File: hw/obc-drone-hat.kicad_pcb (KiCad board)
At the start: 2 copper layers, 65 x 56.5 mm, 0 parts

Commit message: hw: wonring on NET
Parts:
- added C1: 0.1, Capacitor_SMD:C_0603_1608Metric, F.Cu at (270.9, 119.1)
- added C10: 0.1, Capacitor_SMD:C_0603_1608Metric, F.Cu at (284.8, 105.7)
- added C11: 0.1, Capacitor_SMD:C_0603_1608Metric, F.Cu at (339.0, 99.8)
- added C12: 0.1, Capacitor_SMD:C_0603_1608Metric, F.Cu at (347.7, 94.1)
- added C13: 0.1, Capacitor_SMD:C_0603_1608Metric, F.Cu at (335.6, 99.8)
- added C14: 0.1, Capacitor_SMD:C_0603_1608Metric, F.Cu at (303.1, 117.5)
- added C15: 0.01, Capacitor_SMD:C_0603_1608Metric, F.Cu at (286.8, 81.6)
- added C16: 10.0 50V, Capacitor_SMD:C_1206_3216Metric_Pad1.24x1.80mm_HandSolder, F.Cu at (252.7, 84.1)
- added C17: 10.0 50V, Capacitor_SMD:C_1206_3216Metric_Pad1.24x1.80mm_HandSolder, F.Cu at (271.4, 82.4)
- added C18: 0.47, Capacitor_SMD:C_1206_3216Metric_Pad1.24x1.80mm_HandSolder, F.Cu at (259.1, 84.1)
- added C19: 1000.0 uF 10 V, Capacitor_SMD:CP_Elec_10x10.5, F.Cu at (188.0, 99.0)
- added C2: 0.1, Capacitor_SMD:C_0603_1608Metric, F.Cu at (291.6, 108.5)
- added C3: 0.1, Capacitor_SMD:C_0603_1608Metric, F.Cu at (293.2, 97.8)
- added C4: 0.1, Capacitor_SMD:C_0603_1608Metric, F.Cu at (277.7, 116.7)
- added C5: 0.1, Capacitor_SMD:C_0603_1608Metric, F.Cu at (270.9, 113.7)
- added C6: 0.1, Capacitor_SMD:C_0603_1608Metric, F.Cu at (293.2, 103.2)
- added C7: 0.1, Capacitor_SMD:C_0603_1608Metric, F.Cu at (296.6, 97.8)
- added C8: 0.1, Capacitor_SMD:C_0603_1608Metric, F.Cu at (282.8, 111.0)
- added C9: 0.1, Capacitor_SMD:C_0603_1608Metric, F.Cu at (288.2, 105.7)
- added DA1: NCP361SN, Package_TO_SOT_SMD:SOT-23-5_HandSoldering, F.Cu at (287.3, 99.1)
- added DA2: LM2678SX-5.0/NOPB, Package_TO_SOT_SMD:TO-263-7_TabPin4, F.Cu at (185.0, 125.0)
- added DD1: CAT24C256WI-GT3, Package_SO:SO-8_5.3x6.2mm_P1.27mm, F.Cu at (308.6, 100.3)
- added DD2: STM32F030CCTx, Package_QFP:LQFP-48_7x7mm_P0.5mm, F.Cu at (281.0, 138.0)
- added DD3: NC7SZ157P6X, Package_TO_SOT_SMD:SOT-363_SC-70-6_Handsoldering, F.Cu at (267.2, 108.0)
- added DD4: MAX3109, Package_DFN_QFN:QFN-32-1EP_5x5mm_P0.5mm_EP3.45x3.45mm, F.Cu at (337.4, 153.7)
- added DD5: DS3231, Package_SO:SOIC-16W_7.5x10.3mm_P1.27mm, F.Cu at (350.6, 156.2)
- added HL1: WS2812B, LED_SMD:LED_WS2812B_PLCC4_5.0x5.0mm_P3.2mm, F.Cu at (265.3, 115.6)
- added JP1: Jumper_3_Open, Jumper:SolderJumper-3_P1.3mm_Open_RoundedPad1.0x1.5mm, F.Cu at (339.9, 94.2)
- added L1: 12 uH SRR1208-120ML, Inductor_SMD:L_12x12mm_H8mm, F.Cu at (187.0, 111.0)
- added R1: 1k, Resistor_SMD:R_0603_1608Metric, F.Cu at (303.0, 108.1)
- added R10: 10k, Resistor_SMD:R_0603_1608Metric, F.Cu at (284.4, 116.4)
- added R11: 10k, Resistor_SMD:R_0603_1608Metric, F.Cu at (286.2, 111.0)
- added R12: 10k, Resistor_SMD:R_0603_1608Metric, F.Cu at (295.1, 113.9)
- added R13: 4.7k, Resistor_SMD:R_0603_1608Metric, F.Cu at (291.5, 113.9)
- added R14: 10k, Resistor_SMD:R_0603_1608Metric, F.Cu at (287.9, 116.4)
- added R15: nc, Resistor_SMD:R_0603_1608Metric, F.Cu at (347.7, 99.4)
- added R16: 10k, Resistor_SMD:R_0603_1608Metric, F.Cu at (342.5, 99.8)
- added R2: 3.9k, Resistor_SMD:R_0603_1608Metric, F.Cu at (317.7, 105.7)
- added R3: 3.9k, Resistor_SMD:R_0603_1608Metric, F.Cu at (306.6, 108.1)
- added R4: 10k, Resistor_SMD:R_0603_1608Metric, F.Cu at (325.9, 97.8)
- added R5: 47k, Resistor_SMD:R_0603_1608Metric, F.Cu at (310.1, 108.1)
- added R6: 47k, Resistor_SMD:R_0603_1608Metric, F.Cu at (294.9, 108.5)
- added R7: 10k, Resistor_SMD:R_0603_1608Metric, F.Cu at (274.3, 116.7)
- added R8: 47k, Resistor_SMD:R_0603_1608Metric, F.Cu at (296.6, 103.2)
- added R9: 10k, Resistor_SMD:R_0603_1608Metric, F.Cu at (281.0, 116.7)
- added SW1: SW_DIP_x04, Button_Switch_THT:SW_DIP_SPSTx04_Slide_9.78x12.34mm_W7.62mm_P2.54mm, F.Cu at (154.0, 93.0)
- added VT1: DMG2305UX, Package_TO_SOT_SMD:SOT-23_Handsoldering, F.Cu at (368.5, 116.5)
- added VT2: DMMT5401, Package_TO_SOT_SMD:SOT-23-6_Handsoldering, F.Cu at (320.0, 99.1)
- added VT3: DMG2305UX, Package_TO_SOT_SMD:SOT-23_Handsoldering, F.Cu at (368.5, 126.6)
- added XP11: UNUSED PINS, Connector_PinSocket_2.00mm:PinSocket_2x05_P2.00mm_Vertical, F.Cu at (327.0, 59.0)
- added XP12: PWR-5V, Connector_JST:JST_PH_B2B-PH-K_1x02_P2.00mm_Vertical, F.Cu at (338.8, 67.9)
- added XP13: PWR-5V, Connector_JST:JST_PH_B2B-PH-K_1x02_P2.00mm_Vertical, F.Cu at (339.0, 76.0)
- added XP2: FrSky-XSR, Connector_JST:JST_GH_SM06B-GHS-TB_1x06-1MP_P1.25mm_Horizontal, F.Cu at (150.0, 137.0)
- added XP3: DC-Debug, Connector_JST:JST_GH_BM06B-GHS-TBT_1x06-1MP_P1.25mm_Vertical, F.Cu at (225.0, 89.0)
- added XP4: FAN, Connector:FanPinHeader_1x03_P2.54mm_Vertical, F.Cu at (276.0, 99.6)
- added XP5: CPPM OUT, Connector_JST:JST_PH_B2B-PH-K_1x02_P2.00mm_Vertical, F.Cu at (159.0, 136.0)
- added XP6: TELEM1, Connector_JST:JST_GH_SM06B-GHS-TB_1x06-1MP_P1.25mm_Horizontal, F.Cu at (134.0, 97.0)
- added XP7: TELEM2, Connector_JST:JST_GH_SM06B-GHS-TB_1x06-1MP_P1.25mm_Horizontal, F.Cu at (134.0, 109.0)
- added XP8: CFG ID, Connector_JST:JST_PH_B4B-PH-K_1x04_P2.00mm_Vertical, F.Cu at (160.0, 94.0)
- added XP9: RPI-CON, Connector_JST:JST_GH_BM06B-GHS-TBT_1x06-1MP_P1.25mm_Vertical, F.Cu at (213.0, 89.0)
- added ZQ1: ASFL1-24.000MHZ-EC-T, Crystal:Crystal_SMD_Abracon_ABM3B-4Pin_5.0x3.2mm, F.Cu at (323.9, 152.8)

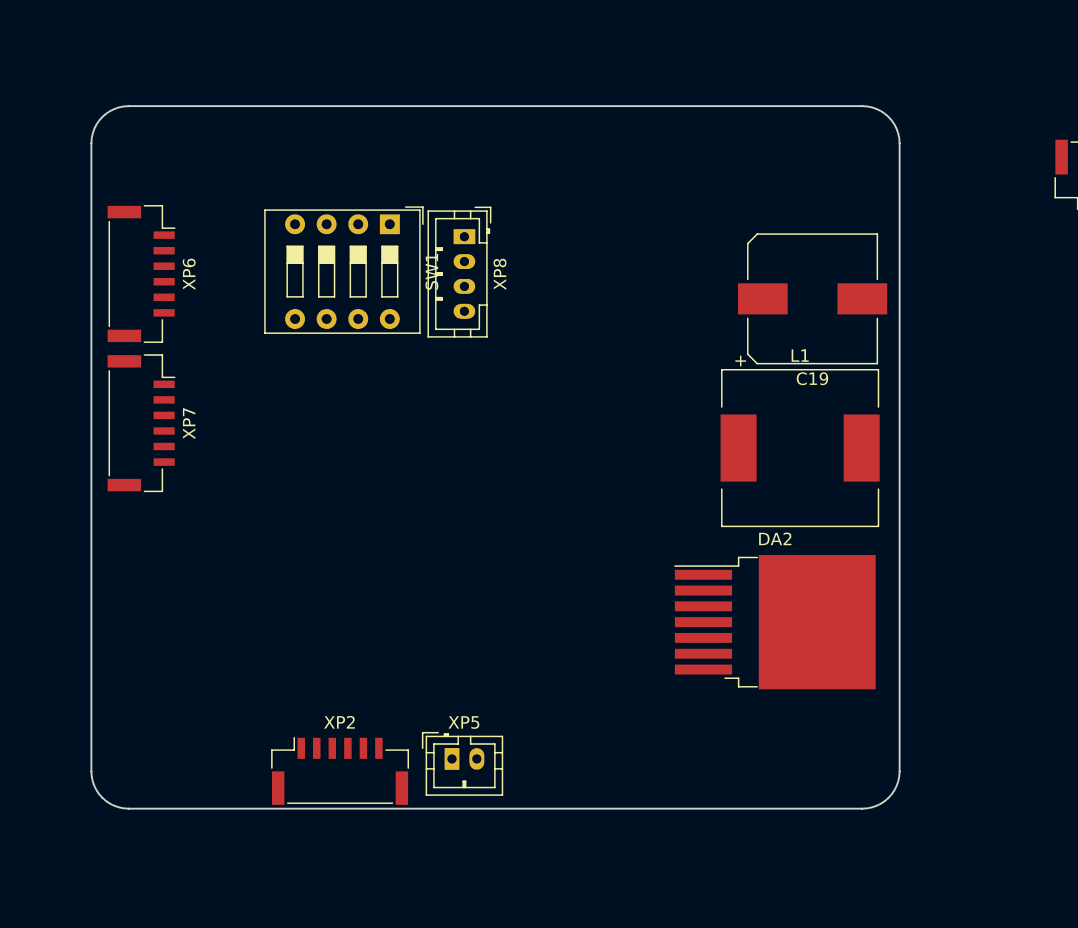
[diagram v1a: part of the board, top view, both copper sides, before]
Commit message: hw: add mounting holes
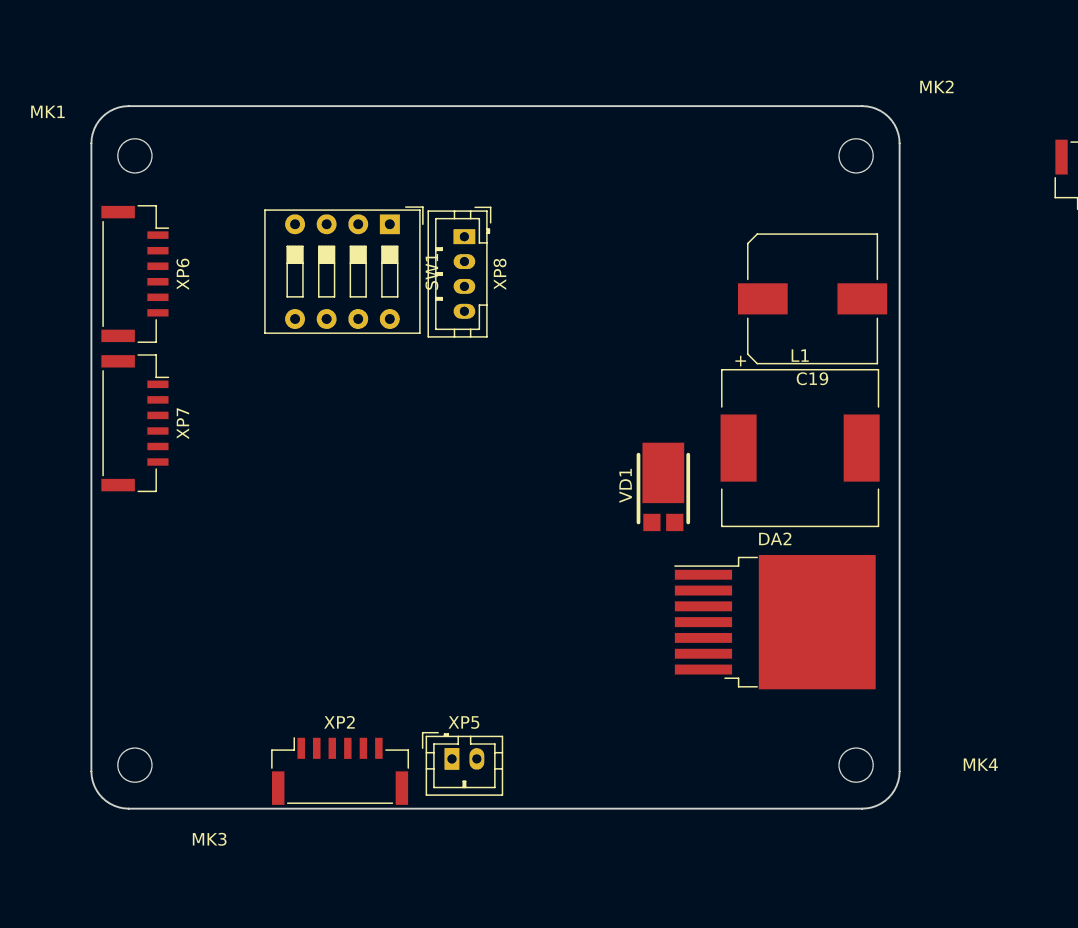
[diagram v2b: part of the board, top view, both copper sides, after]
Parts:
- added MK1: Mounting_Hole, hat:M2.5_Mounting_Hole, F.Cu at (133.5, 87.5)
- added MK2: Mounting_Hole, hat:M2.5_Mounting_Hole, F.Cu at (191.5, 87.5)
- added MK3: Mounting_Hole, hat:M2.5_Mounting_Hole, F.Cu at (133.5, 136.5)
- added MK4: Mounting_Hole, hat:M2.5_Mounting_Hole, F.Cu at (191.5, 136.5)
- added VD1: PDS760-13, hat:D-PowerDI-5, F.Cu at (176.0, 117.0)
- moved XP6 0.50 mm to (133.5, 97.0)
- moved XP7 0.50 mm to (133.5, 109.0)
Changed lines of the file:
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@@
   (general
     (thickness 1.6)
-    (drawings 8)
+    (drawings 13)
     (tracks 0)
     (zones 0)
-    (modules 61)
+    (modules 66)
     (nets 55)
   )
@@
   )
   (module Connector_JST:JST_GH_SM06B-GHS-TB_1x06-1MP_P1.25mm_Horizontal (layer F.Cu)
-    (at 134 97 270)
+    (at 133.5 97 270)
     (descr "JST GH series connector, SM06B-GHS-TB (http://www.jst-mfg.com/product/pdf/eng/eGH.pdf), generated with kicad-footprint-generator")
     (tags "connector JST GH top entry")
@@
   )
   (module Connector_JST:JST_GH_SM06B-GHS-TB_1x06-1MP_P1.25mm_Horizontal (layer F.Cu)
-    (at 134 109 270)
+    (at 133.5 109 270)
     (descr "JST GH series connector, SM06B-GHS-TB (http://www.jst-mfg.com/product/pdf/eng/eGH.pdf), generated with kicad-footprint-generator")
     (tags "connector JST GH top entry")
@@
     )
   )
+  (module hat:D-PowerDI-5 (layer F.Cu)
+    (at 176 116.982)
+    (fp_text reference VD1 (at -3 -3 90) (layer F.SilkS)
+      (effects (font (size 1 1) (thickness 0.15)))
+    )
+    (fp_text value PDS760-13 (at 0 2) (layer F.Fab)
+      (effects (font (size 1 1) (thickness 0.15)))
+    )
+    (fp_line (start 2 -5.45) (end 2 0) (layer F.SilkS) (width 0.3))
+    (fp_line (start -2 -5.45) (end -2 0) (layer F.SilkS) (width 0.3))
+    (pad 2 smd rect (at -0.92 0) (size 1.39 1.4) (layers F.Cu F.Paste F.Mask)
+      (net 1 GND))
+    (pad 2 smd rect (at 0.92 0) (size 1.39 1.4) (layers F.Cu F.Paste F.Mask)
+      (net 1 GND))
+    (pad 1 smd rect (at 0 -3.982) (size 3.36 4.86) (layers F.Cu F.Paste F.Mask)
+      (net 10 /DC-DC/VSW))
+  )
+  (module hat:M2.5_Mounting_Hole (layer F.Cu)
+    (at 133.5 87.5)
+    (fp_text reference MK1 (at -7 -3.5) (layer F.SilkS)
+      (effects (font (size 1 1) (thickness 0.15)))
+    )
+    (fp_text value Mounting_Hole (at -10.5 -2) (layer F.Fab)
+      (effects (font (size 1 1) (thickness 0.15)))
+    )
+    (pad "" np_thru_hole circle (at 0 0) (size 2.75 2.75) (drill 2.75) (layers *.Cu *.Mask)
+      (solder_mask_margin 1.8) (clearance 1.8))
+  )
+  (module hat:M2.5_Mounting_Hole (layer F.Cu)
+    (at 191.5 87.5)
+    (fp_text reference MK2 (at 6.5 -5.5) (layer F.SilkS)
+      (effects (font (size 1 1) (thickness 0.15)))
+    )
+    (fp_text value Mounting_Hole (at 10 -4) (layer F.Fab)
+      (effects (font (size 1 1) (thickness 0.15)))
+    )
+    (pad "" np_thru_hole circle (at 0 0) (size 2.75 2.75) (drill 2.75) (layers *.Cu *.Mask)
+      (solder_mask_margin 1.8) (clearance 1.8))
+  )
+  (module hat:M2.5_Mounting_Hole (layer F.Cu)
+    (at 133.5 136.5)
+    (fp_text reference MK3 (at 6 6) (layer F.SilkS)
+      (effects (font (size 1 1) (thickness 0.15)))
+    )
+    (fp_text value Mounting_Hole (at 6.5 7.5) (layer F.Fab)
+      (effects (font (size 1 1) (thickness 0.15)))
+    )
+    (pad "" np_thru_hole circle (at 0 0) (size 2.75 2.75) (drill 2.75) (layers *.Cu *.Mask)
+      (solder_mask_margin 1.8) (clearance 1.8))
+  )
+  (module hat:M2.5_Mounting_Hole (layer F.Cu)
+    (at 191.5 136.5)
+    (fp_text reference MK4 (at 10 0) (layer F.SilkS)
+      (effects (font (size 1 1) (thickness 0.15)))
+    )
+    (fp_text value Mounting_Hole (at 10 1.5) (layer F.Fab)
+      (effects (font (size 1 1) (thickness 0.15)))
+    )
+    (pad "" np_thru_hole circle (at 0 0) (size 2.75 2.75) (drill 2.75) (layers *.Cu *.Mask)
+      (solder_mask_margin 1.8) (clearance 1.8))
+  )
+  (dimension 58 (width 0.3) (layer Dwgs.User)
+    (gr_text "58,000 мм" (at 162.5 148.6) (layer Dwgs.User)
+      (effects (font (size 1.5 1.5) (thickness 0.3)))
+    )
+    (feature1 (pts (xy 191.5 136.5) (xy 191.5 147.086421)))
+    (feature2 (pts (xy 133.5 136.5) (xy 133.5 147.086421)))
+    (crossbar (pts (xy 133.5 146.5) (xy 191.5 146.5)))
+    (arrow1a (pts (xy 191.5 146.5) (xy 190.373496 147.086421)))
+    (arrow1b (pts (xy 191.5 146.5) (xy 190.373496 145.913579)))
+    (arrow2a (pts (xy 133.5 146.5) (xy 134.626504 147.086421)))
+    (arrow2b (pts (xy 133.5 146.5) (xy 134.626504 145.913579)))
+  )
+  (dimension 3.5 (width 0.3) (layer Dwgs.User)
+    (gr_text "3,500 мм" (at 131.75 148.6) (layer Dwgs.User)
+      (effects (font (size 1.5 1.5) (thickness 0.3)))
+    )
+    (feature1 (pts (xy 130 136.5) (xy 130 147.086421)))
+    (feature2 (pts (xy 133.5 136.5) (xy 133.5 147.086421)))
+    (crossbar (pts (xy 133.5 146.5) (xy 130 146.5)))
+    (arrow1a (pts (xy 130 146.5) (xy 131.126504 145.913579)))
+    (arrow1b (pts (xy 130 146.5) (xy 131.126504 147.086421)))
+    (arrow2a (pts (xy 133.5 146.5) (xy 132.373496 145.913579)))
+    (arrow2b (pts (xy 133.5 146.5) (xy 132.373496 147.086421)))
+  )
+  (dimension 3.5 (width 0.3) (layer Dwgs.User)
+    (gr_text "3,500 мм" (at 116.4 138.25 90) (layer Dwgs.User)
+      (effects (font (size 1.5 1.5) (thickness 0.3)))
+    )
+    (feature1 (pts (xy 133.5 136.5) (xy 117.913579 136.5)))
+    (feature2 (pts (xy 133.5 140) (xy 117.913579 140)))
+    (crossbar (pts (xy 118.5 140) (xy 118.5 136.5)))
+    (arrow1a (pts (xy 118.5 136.5) (xy 119.086421 137.626504)))
+    (arrow1b (pts (xy 118.5 136.5) (xy 117.913579 137.626504)))
+    (arrow2a (pts (xy 118.5 140) (xy 119.086421 138.873496)))
+    (arrow2b (pts (xy 118.5 140) (xy 117.913579 138.873496)))
+  )
+  (dimension 49 (width 0.3) (layer Dwgs.User)
+    (gr_text "49,000 мм" (at 116.4 112.014924 270) (layer Dwgs.User)
+      (effects (font (size 1.5 1.5) (thickness 0.3)))
+    )
+    (feature1 (pts (xy 133.5 136.514924) (xy 117.913579 136.514924)))
+    (feature2 (pts (xy 133.5 87.514924) (xy 117.913579 87.514924)))
+    (crossbar (pts (xy 118.5 87.514924) (xy 118.5 136.514924)))
+    (arrow1a (pts (xy 118.5 136.514924) (xy 117.913579 135.38842)))
+    (arrow1b (pts (xy 118.5 136.514924) (xy 119.086421 135.38842)))
+    (arrow2a (pts (xy 118.5 87.514924) (xy 117.913579 88.641428)))
+    (arrow2b (pts (xy 118.5 87.514924) (xy 119.086421 88.641428)))
+  )
+  (dimension 65 (width 0.3) (layer Dwgs.User)
+    (gr_text "65,000 мм" (at 162.5 70.9) (layer Dwgs.User)
+      (effects (font (size 1.5 1.5) (thickness 0.3)))
+    )
+    (feature1 (pts (xy 195 90) (xy 195 72.413579)))
+    (feature2 (pts (xy 130 90) (xy 130 72.413579)))
+    (crossbar (pts (xy 130 73) (xy 195 73)))
+    (arrow1a (pts (xy 195 73) (xy 193.873496 73.586421)))
+    (arrow1b (pts (xy 195 73) (xy 193.873496 72.413579)))
+    (arrow2a (pts (xy 130 73) (xy 131.126504 73.586421)))
+    (arrow2b (pts (xy 130 73) (xy 131.126504 72.413579)))
+  )
   (gr_arc (start 192 137) (end 195 137) (angle 90) (layer Edge.Cuts) (width 0.15))
